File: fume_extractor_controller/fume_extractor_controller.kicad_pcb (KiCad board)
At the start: 4 copper layers, 40 x 46.1 mm, 32 parts, among them J1 Conn_01x02, J2 Conn_01x04, J3 Conn_01x02_Pin, Q1 Q_NMOS_GDS, SW1 SW_SPDT, U1 NE555P, U2 NE555P

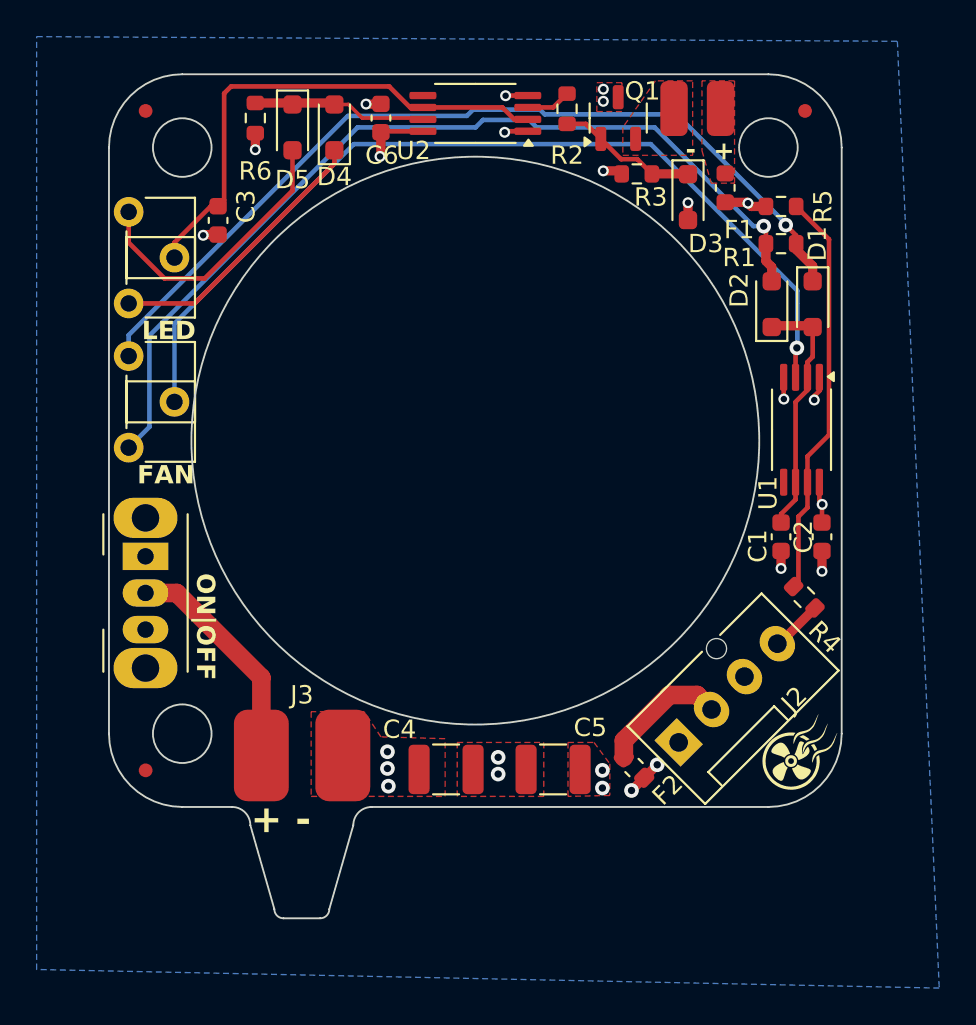
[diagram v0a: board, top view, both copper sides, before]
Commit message: Added part numbers and changed mosfet from gds to gsd.
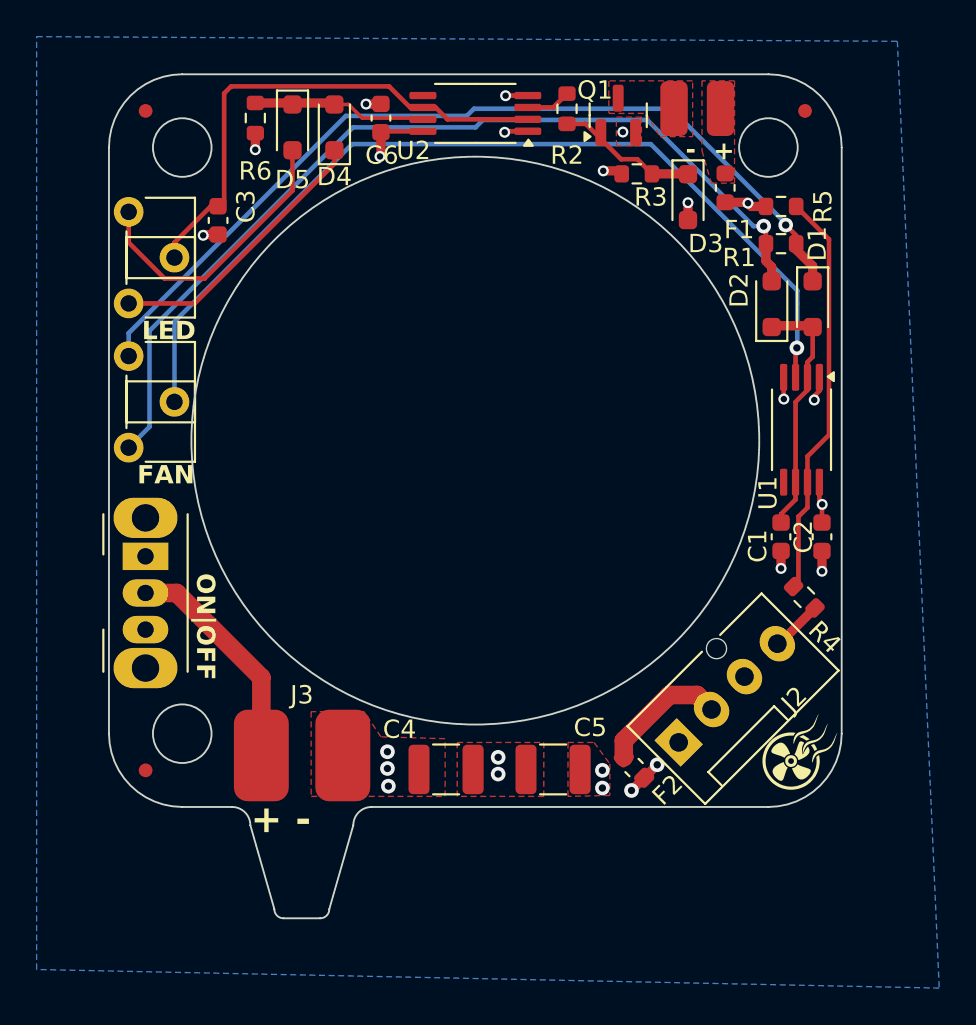
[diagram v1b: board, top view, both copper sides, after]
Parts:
- F1, F2: value 1.5A -> 1A
- J3: value Conn_01x02_Pin -> 12V 1A
- Q1: value Q_NMOS_GDS -> Q_NMOS_GSD; footprint Package_TO_SOT_SMD:SOT-23-3 -> Package_TO_SOT_SMD:SOT-23
- moved Q1 0.15 mm to (177.8, 72.2)
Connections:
- Q1 pad 2: /GND_PWM -> GND
- Q1 pad 3: GND -> /GND_PWM
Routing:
- net GND: vias 15 -> 14

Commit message: v1_20052024 added. Production docs generated.
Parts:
- added REF**: WEEE-Logo_4.2x6mm_SilkScreen, Symbol:WEEE-Logo_4.2x6mm_SilkScreen, B.Cu at (187.5, 81.5)
- added REF**: ESD-Logo_6.6x6mm_SilkScreen, Symbol:ESD-Logo_6.6x6mm_SilkScreen, B.Cu at (160.5, 106.5)
- C5: value 22uF -> 47uF
- J2: value Conn_01x04 -> MX-47053-1000
- R2, R4: value 200 -> 220
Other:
- board text added: "JLCJLCJLCJLC"
- board text added: "V1_20052024"
